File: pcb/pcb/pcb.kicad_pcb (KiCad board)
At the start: 2 copper layers, 58.4 x 44.4 mm, 26 parts, among them J1 UART, J2 Barrel_Jack, J3 Stepper, SW1 RESET, SW2 FLASH, U1 ESP32-WROOM-32, U2 TSR_1-2433

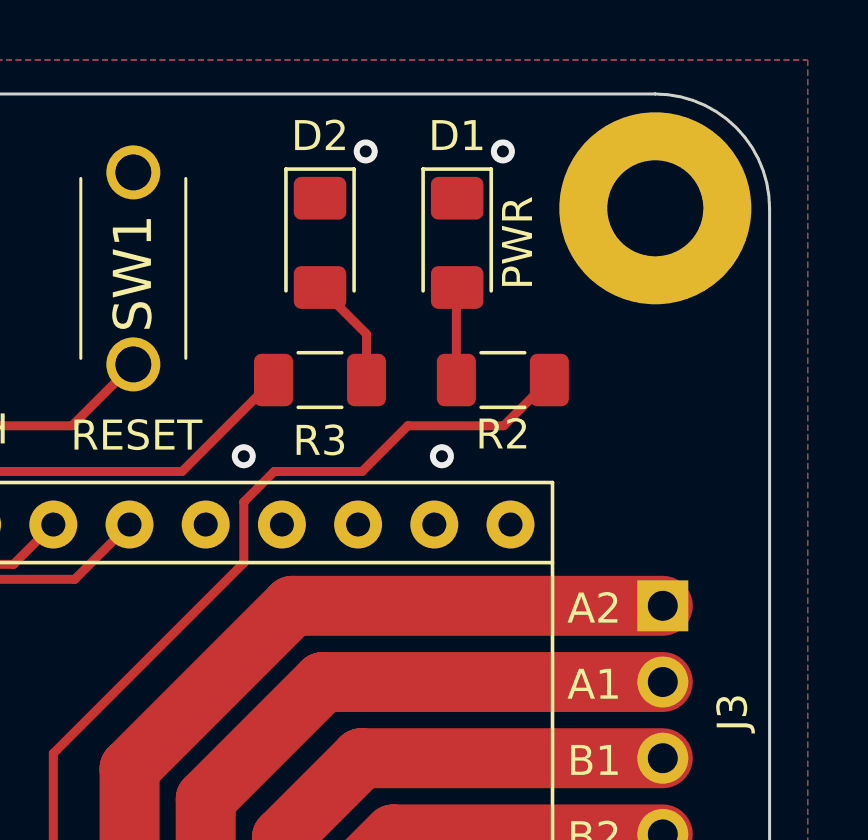
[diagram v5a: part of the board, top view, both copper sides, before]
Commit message: add more silkscreen
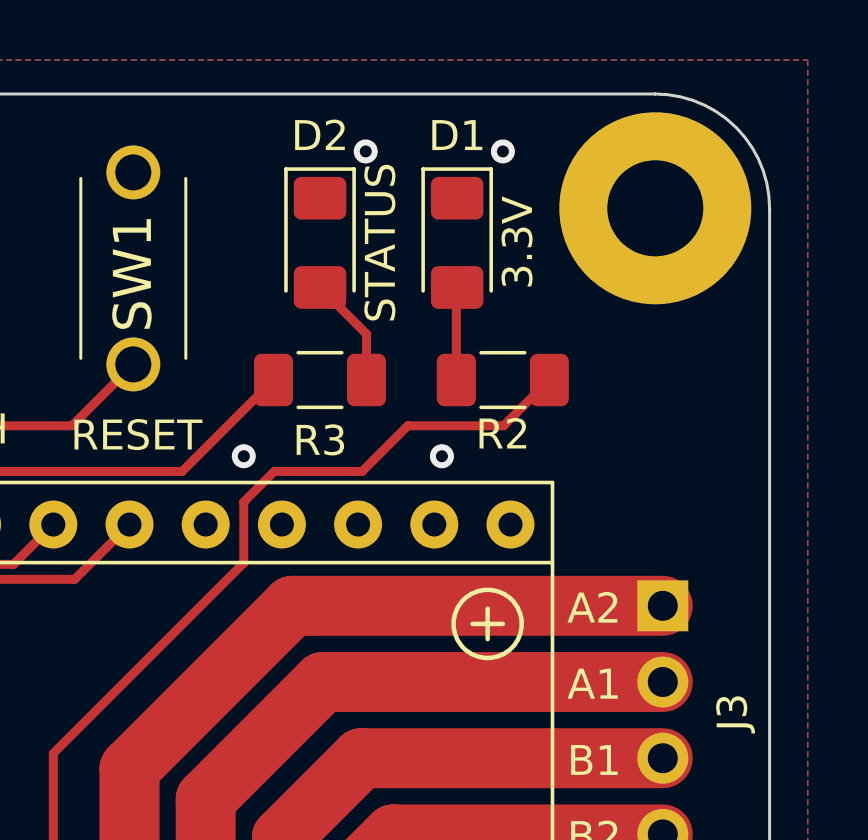
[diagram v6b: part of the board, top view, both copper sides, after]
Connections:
- U1 pad 39: GND -> (no net)
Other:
- board text added: "3.3V"
- board text added: "STATUS"
- board text removed: "PWR"
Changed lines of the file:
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@@
     (property "Sheetfile" "pcb.kicad_sch")
     (property "Sheetname" "")
-    (attr exclude_from_pos_files)
+    (attr exclude_from_pos_files exclude_from_bom)
     (fp_text reference "H3" (at 0 -4.2) (layer "F.SilkS") hide
       (effects (font (size 1 1) (thickness 0.15)))
@@
       (net 2 "GND") (pinfunction "GND") (pintype "passive"))
     (pad "39" smd rect (at -1 -0.755 90) (size 5 5) (layers "F.Cu" "F.Paste" "F.Mask")
-      (net 2 "GND") (pinfunction "GND") (pintype "passive") (zone_connect 0) (thermal_width 0.1))
+      (pinfunction "GND") (pintype "passive") (zone_connect 0) (thermal_width 0.1))
     (model "${KICAD6_3DMODEL_DIR}/RF_Module.3dshapes/ESP32-WROOM-32.wrl"
       (offset (xyz 0 0 0))
@@
     (property "Sheetfile" "pcb.kicad_sch")
     (property "Sheetname" "")
-    (attr exclude_from_pos_files)
+    (attr exclude_from_pos_files exclude_from_bom)
     (fp_text reference "H1" (at 0 -4.2) (layer "F.SilkS") hide
       (effects (font (size 1 1) (thickness 0.15)))
@@
     )
   )
+  (gr_line (start 126.492 60.96) (end 126.492 61.976) (layer "F.SilkS") (width 0.15))
+  (gr_line (start 125.984 61.468) (end 127 61.468) (layer "F.SilkS") (width 0.15))
+  (gr_circle (center 126.492 61.468) (end 127.508 60.96) (layer "F.SilkS") (width 0.15) (fill none))
   (gr_circle (center 130.81 50.155) (end 130.81 50.155) (layer "Edge.Cuts") (width 0.1) (fill none))
   (gr_arc (start 81.28 88.255) (mid 78.585923 87.139077) (end 77.47 84.445) (layer "Edge.Cuts") (width 0.1))
@@
     (effects (font (size 1 1) (thickness 0.15)))
   )
+  (gr_text "STATUS" (at 122.936 48.768 90) (layer "F.SilkS")
+    (effects (font (size 1 1) (thickness 0.15)))
+  )
   (gr_text "B1" (at 130.048 66.04) (layer "F.SilkS")
     (effects (font (size 1 1) (thickness 0.15)))
@@
     (effects (font (size 1 1) (thickness 0.15)))
   )
-  (gr_text "PWR" (at 127.508 48.768 90) (layer "F.SilkS")
-    (effects (font (size 1 1) (thickness 0.15)))
-  )
+  (gr_text "3.3V" (at 127.508 48.768 90) (layer "F.SilkS")
+    (effects (font (size 1 1) (thickness 0.15)))
+  )

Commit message: small layout tweaks
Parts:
- moved REF** 2.09 mm to (86.9, 82.8)
- moved C5 0.85 mm to (110.8, 76.2)
- moved C6 0.83 mm to (110.7, 84.8)
- moved J2 0.62 mm to (120.4, 75.8)
- turned R2 to 0 degrees
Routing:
- net +3V3: track 63.0 -> 59.7 mm
- net Net-(D1-Pad2): track 3.10 -> 5.08 mm
- net Net-(C6-Pad1): track 8.27 -> 9.42 mm
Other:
- board text added: "twilight rev1.0"
- board text removed: "twilight v1.0"

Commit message: add octopus icon
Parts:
- added G***: LOGO, customsymbols:octopus, F.Cu at (94.2, 83.1)
- moved REF** 1.09 mm to (87.2, 81.8)
